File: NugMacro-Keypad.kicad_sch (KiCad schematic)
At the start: 14 parts

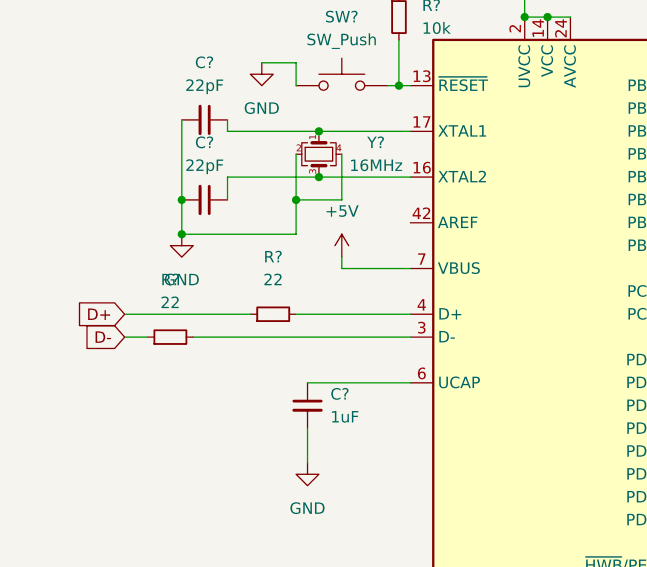
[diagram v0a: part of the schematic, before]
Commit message: Reset circuit in schema
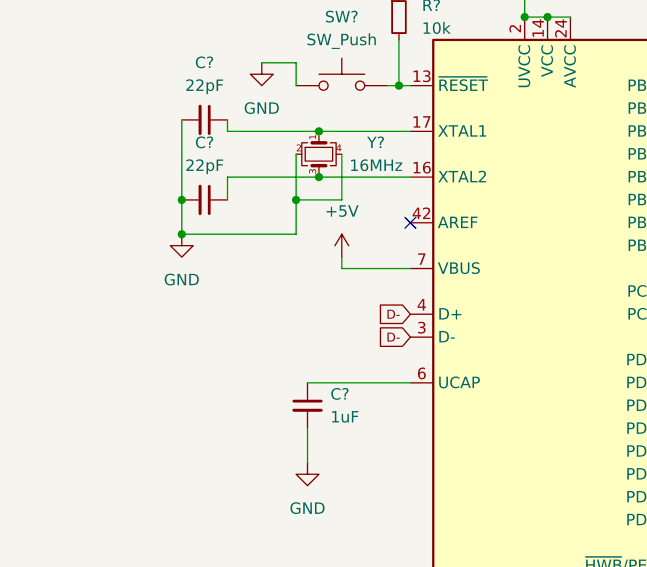
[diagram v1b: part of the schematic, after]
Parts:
- removed R? (x2): 22, symbol Device:R_Small
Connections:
- net D-: now also U?.3 (D-), U?.4 (D+)
- no-connect marks 0 -> 1
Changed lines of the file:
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@@
   (junction (at 168.91 120.65) (diameter 0) (color 0 0 0 0)
   )
+  (no_connect (at 195.58 71.12))
   (wire (pts (xy 195.58 76.2) (xy 187.96 76.2))
     (stroke (width 0) (type default) (color 0 0 0 0))
   )
-  (wire (pts (xy 182.88 81.28) (xy 195.58 81.28))
-    (stroke (width 0) (type default) (color 0 0 0 0))
-  )
   (wire (pts (xy 185.42 60.96) (xy 195.58 60.96))
     (stroke (width 0) (type default) (color 0 0 0 0))
@@
     (stroke (width 0) (type default) (color 0 0 0 0))
   )
-  (wire (pts (xy 163.83 81.28) (xy 177.8 81.28))
-    (stroke (width 0) (type default) (color 0 0 0 0))
-  )
   (wire (pts (xy 185.42 66.04) (xy 195.58 66.04))
     (stroke (width 0) (type default) (color 0 0 0 0))
@@
     (stroke (width 0) (type default) (color 0 0 0 0))
   )
-  (wire (pts (xy 163.83 83.82) (xy 166.37 83.82))
-    (stroke (width 0) (type default) (color 0 0 0 0))
-  )
   (wire (pts (xy 168.91 120.65) (xy 173.99 120.65))
     (stroke (width 0) (type default) (color 0 0 0 0))
@@
     (stroke (width 0) (type default) (color 0 0 0 0))
   )
-  (wire (pts (xy 171.45 83.82) (xy 195.58 83.82))
-    (stroke (width 0) (type default) (color 0 0 0 0))
-  )
   (wire (pts (xy 194.31 50.8) (xy 194.31 55.88))
     (stroke (width 0) (type default) (color 0 0 0 0))
@@
     (stroke (width 0) (type default) (color 0 0 0 0))
   )
-  (global_label "D-" (shape input) (at 163.83 83.82 180) (fields_autoplaced)
-    (effects (font (size 1.27 1.27)) (justify right))
-    (property "Intersheet References" "${INTERSHEET_REFS}" (id 0) (at 158.5745 83.7406 0)
-      (effects (font (size 1.27 1.27)) (justify right) hide)
-    )
-  )
-  (global_label "D+" (shape input) (at 163.83 81.28 180) (fields_autoplaced)
-    (effects (font (size 1.27 1.27)) (justify right))
-    (property "Intersheet References" "${INTERSHEET_REFS}" (id 0) (at 158.5745 81.2006 0)
-      (effects (font (size 1.27 1.27)) (justify right) hide)
-    )
-  )
-  (symbol (lib_id "Device:R_Small") (at 180.34 81.28 90) (unit 1)
-    (in_bom yes) (on_board yes) (fields_autoplaced)
-    (property "Reference" "R?" (id 0) (at 180.34 74.93 90))
-    (property "Value" "22" (id 1) (at 180.34 77.47 90))
-    (property "Footprint" "" (id 2) (at 180.34 81.28 0)
-      (effects (font (size 1.27 1.27)) hide)
-    )
-    (property "Datasheet" "~" (id 3) (at 180.34 81.28 0)
-      (effects (font (size 1.27 1.27)) hide)
-    )
-    (pin "1")
-    (pin "2")
+  (global_label "D-" (shape input) (at 195.58 81.28 180) (fields_autoplaced)
+    (effects (font (size 1 1)) (justify right))
+    (property "Intersheet References" "${INTERSHEET_REFS}" (id 0) (at 191.4419 81.2175 0)
+      (effects (font (size 1 1)) (justify right) hide)
+    )
+  )
+  (global_label "D-" (shape input) (at 195.58 83.82 180) (fields_autoplaced)
+    (effects (font (size 1 1)) (justify right))
+    (property "Intersheet References" "${INTERSHEET_REFS}" (id 0) (at 191.4419 83.7575 0)
+      (effects (font (size 1 1)) (justify right) hide)
+    )
   )
   (symbol (lib_id "power:+5V") (at 208.28 41.91 0) (unit 1)
@@
     )
     (property "Datasheet" "~" (id 3) (at 242.57 109.22 0)
-      (effects (font (size 1.27 1.27)) hide)
-    )
-    (pin "1")
-    (pin "2")
-  )
-  (symbol (lib_id "Device:R_Small") (at 168.91 83.82 90) (unit 1)
-    (in_bom yes) (on_board yes) (fields_autoplaced)
-    (property "Reference" "R?" (id 0) (at 168.91 77.47 90))
-    (property "Value" "22" (id 1) (at 168.91 80.01 90))
-    (property "Footprint" "" (id 2) (at 168.91 83.82 0)
-      (effects (font (size 1.27 1.27)) hide)
-    )
-    (property "Datasheet" "~" (id 3) (at 168.91 83.82 0)
       (effects (font (size 1.27 1.27)) hide)
     )
@@
       (reference "C?") (unit 1) (value "0.1uF") (footprint "")
     )
-    (path "/12bf35f5-4e0d-4acb-9c2f-587fb5784310"
-      (reference "R?") (unit 1) (value "22") (footprint "")
-    )
     (path "/4ca06591-1cd5-439b-bf8b-2a0c92e44b1f"
       (reference "R?") (unit 1) (value "10k") (footprint "")
     )
-    (path "/4e408aa6-7198-4329-b6a7-a1cdc51be6fb"
-      (reference "R?") (unit 1) (value "22") (footprint "")
-    )
     (path "/b006b8ac-9a5f-47f9-9de2-1486a1b26a4d"

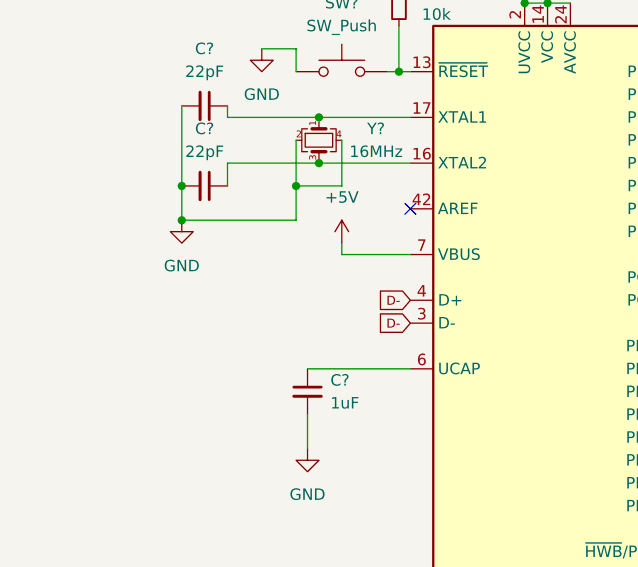
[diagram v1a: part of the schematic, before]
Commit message: fixed fucky wucky on mcu
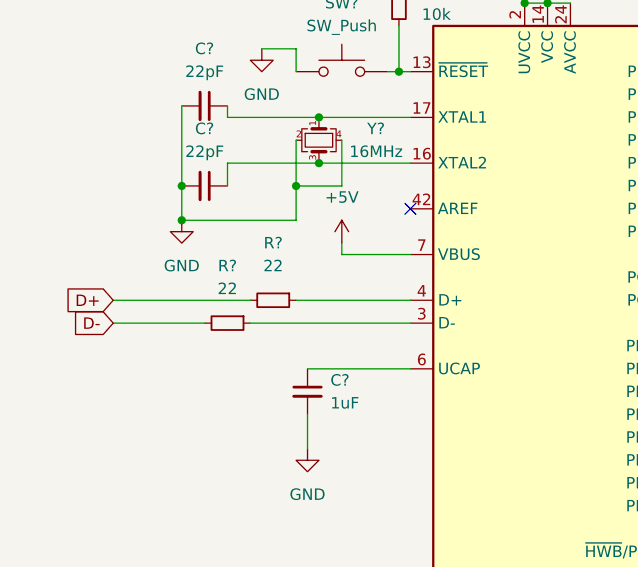
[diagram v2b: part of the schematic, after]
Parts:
- added R? (x2): 22, symbol Device:R_Small
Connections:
- net D-: now also R?.2; no longer U?.3 (D-), U?.4 (D+)
- new net: R?.1, U?.3 (D-)
- new net: R?.1, U?.4 (D+)
- new net D+: R?.2
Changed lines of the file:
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@@
+    (stroke (width 0) (type default) (color 0 0 0 0))
+  )
+  (wire (pts (xy 162.56 81.28) (xy 177.8 81.28))
     (stroke (width 0) (type default) (color 0 0 0 0))
   )
@@
     (stroke (width 0) (type default) (color 0 0 0 0))
   )
+  (wire (pts (xy 177.8 83.82) (xy 195.58 83.82))
+    (stroke (width 0) (type default) (color 0 0 0 0))
+  )
   (wire (pts (xy 194.31 55.88) (xy 195.58 55.88))
     (stroke (width 0) (type default) (color 0 0 0 0))
@@
     (stroke (width 0) (type default) (color 0 0 0 0))
   )
+  (wire (pts (xy 182.88 81.28) (xy 195.58 81.28))
+    (stroke (width 0) (type default) (color 0 0 0 0))
+  )
   (wire (pts (xy 173.99 125.73) (xy 184.15 125.73))
     (stroke (width 0) (type default) (color 0 0 0 0))
@@
     (stroke (width 0) (type default) (color 0 0 0 0))
   )
+  (wire (pts (xy 172.72 83.82) (xy 162.56 83.82))
+    (stroke (width 0) (type default) (color 0 0 0 0))
+  )
   (wire (pts (xy 173.99 120.65) (xy 184.15 120.65))
     (stroke (width 0) (type default) (color 0 0 0 0))
@@
     (stroke (width 0) (type default) (color 0 0 0 0))
   )
-  (global_label "D-" (shape input) (at 195.58 81.28 180) (fields_autoplaced)
-    (effects (font (size 1 1)) (justify right))
-    (property "Intersheet References" "${INTERSHEET_REFS}" (id 0) (at 191.4419 81.2175 0)
-      (effects (font (size 1 1)) (justify right) hide)
-    )
-  )
-  (global_label "D-" (shape input) (at 195.58 83.82 180) (fields_autoplaced)
-    (effects (font (size 1 1)) (justify right))
-    (property "Intersheet References" "${INTERSHEET_REFS}" (id 0) (at 191.4419 83.7575 0)
-      (effects (font (size 1 1)) (justify right) hide)
+  (global_label "D-" (shape input) (at 162.56 83.82 180) (fields_autoplaced)
+    (effects (font (size 1.27 1.27)) (justify right))
+    (property "Intersheet References" "${INTERSHEET_REFS}" (id 0) (at 157.3045 83.7406 0)
+      (effects (font (size 1.27 1.27)) (justify right) hide)
+    )
+  )
+  (global_label "D+" (shape input) (at 162.56 81.28 180) (fields_autoplaced)
+    (effects (font (size 1.27 1.27)) (justify right))
+    (property "Intersheet References" "${INTERSHEET_REFS}" (id 0) (at 157.3045 81.2006 0)
+      (effects (font (size 1.27 1.27)) (justify right) hide)
     )
   )
@@
     (pin "1")
   )
+  (symbol (lib_id "Device:R_Small") (at 175.26 83.82 270) (unit 1)
+    (in_bom yes) (on_board yes) (fields_autoplaced)
+    (property "Reference" "R?" (id 0) (at 175.26 77.47 90))
+    (property "Value" "22" (id 1) (at 175.26 80.01 90))
+    (property "Footprint" "" (id 2) (at 175.26 83.82 0)
+      (effects (font (size 1.27 1.27)) hide)
+    )
+    (property "Datasheet" "~" (id 3) (at 175.26 83.82 0)
+      (effects (font (size 1.27 1.27)) hide)
+    )
+    (pin "1")
+    (pin "2")
+  )
   (symbol (lib_id "Device:Crystal_GND24_Small") (at 185.42 63.5 270) (unit 1)
     (in_bom yes) (on_board yes)
@@
     (pin "3")
     (pin "4")
+  )
+  (symbol (lib_id "Device:R_Small") (at 180.34 81.28 270) (unit 1)
+    (in_bom yes) (on_board yes) (fields_autoplaced)
+    (property "Reference" "R?" (id 0) (at 180.34 74.93 90))
+    (property "Value" "22" (id 1) (at 180.34 77.47 90))
+    (property "Footprint" "" (id 2) (at 180.34 81.28 0)
+      (effects (font (size 1.27 1.27)) hide)
+    )
+    (property "Datasheet" "~" (id 3) (at 180.34 81.28 0)
+      (effects (font (size 1.27 1.27)) hide)
+    )
+    (pin "1")
+    (pin "2")
   )
   (symbol (lib_id "power:GND") (at 168.91 128.27 0) (unit 1)
@@
       (reference "R?") (unit 1) (value "10k") (footprint "")
     )
+    (path "/cc7bf79d-c2b1-41e1-8bd5-f5b360c70387"
+      (reference "R?") (unit 1) (value "22") (footprint "")
+    )
+    (path "/cf7c76cc-f2d3-4702-9419-1efee64a8060"
+      (reference "R?") (unit 1) (value "22") (footprint "")
+    )
     (path "/a573fc8f-1b31-460e-bddf-15f8e483f9e1"
